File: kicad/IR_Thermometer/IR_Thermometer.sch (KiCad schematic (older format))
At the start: 17 parts, among them IC1 PIC16LF19156-I_SP, J1 ICSP Conn, J2 Sensor Conn, J3 Sensor Conn, Q1 SI2323, SW1 Sample Button, SW2 Option Button

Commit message: Updates to schematic
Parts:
- added R5: 100R, Resistors:0603, symbol Device:R
- C1: renamed from C2; value 100nF -> 100n
- C2: renamed from C3; value 100nF -> 100n
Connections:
- net GND: now also R5.1; no longer D1.1 (K)
- new net: D1.1 (K), R5.2
- no-connect marks 10 -> 9
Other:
- note added: "PMOSFET provides\nreverse battery\nprotection"
- moved on the sheet: C1, D1, IC1, R3, R4, SW1, SW2

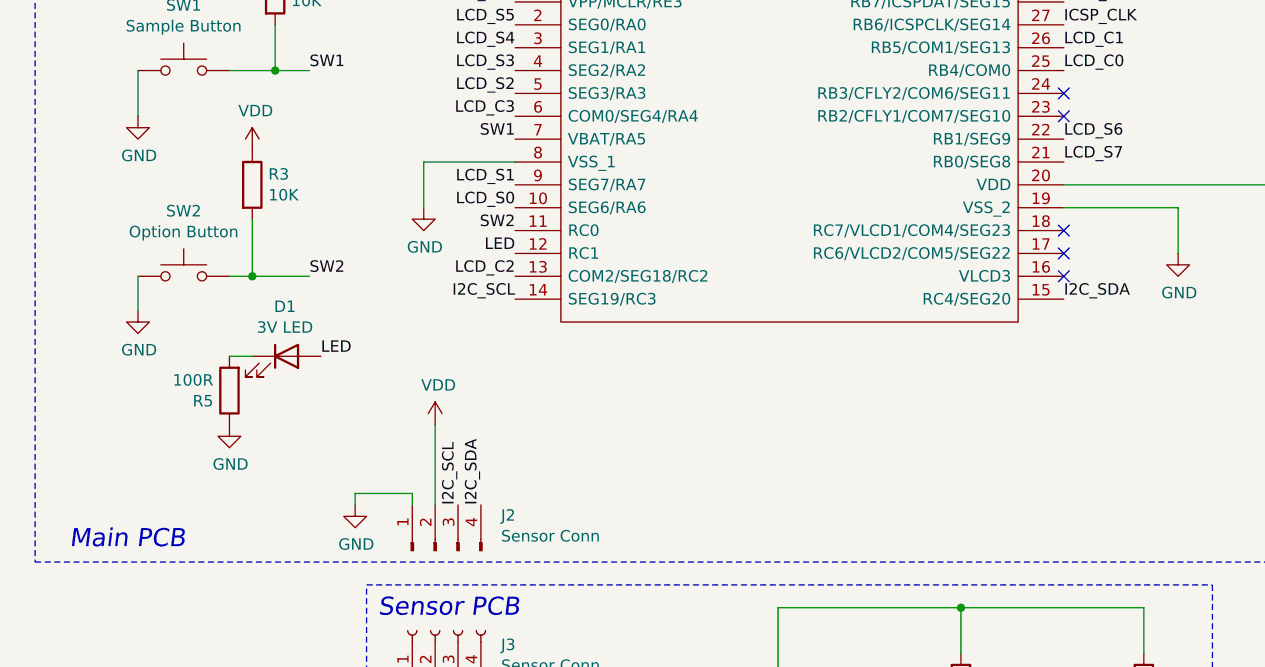
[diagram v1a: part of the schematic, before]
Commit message: Sleep mode implementation
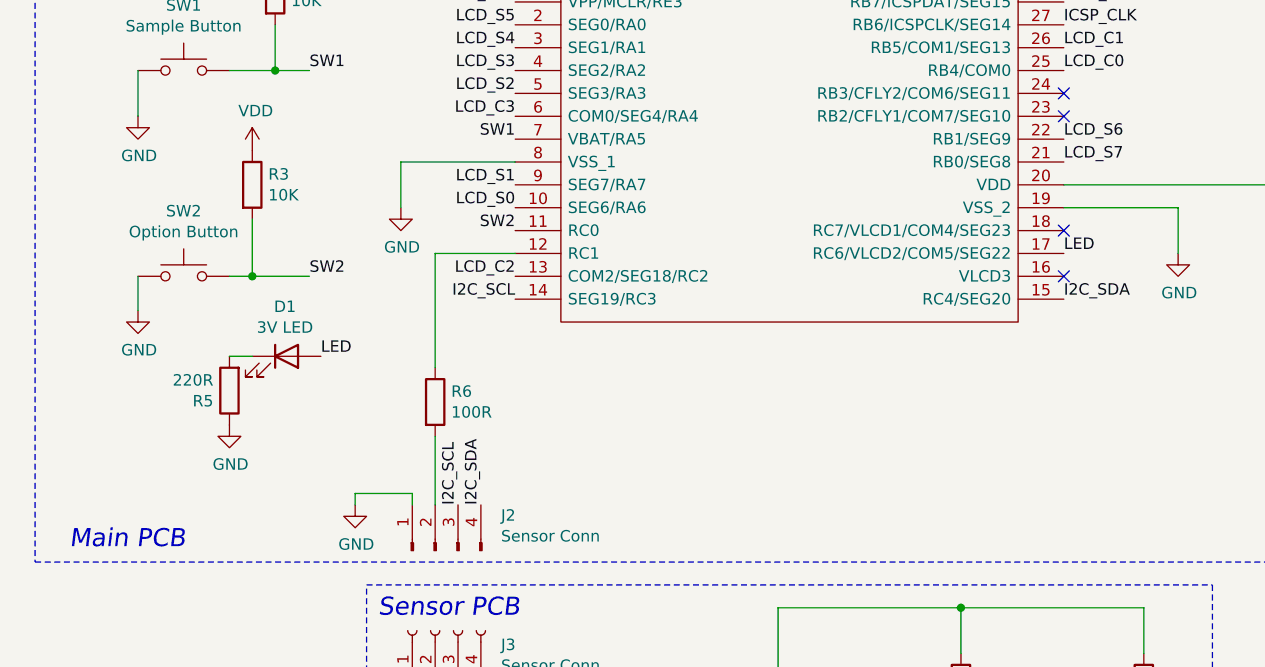
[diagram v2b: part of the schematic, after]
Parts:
- added R6: 100R, Resistor_THT:R_Axial_DIN0207_L6.3mm_D2.5mm_P2.54mm_Vertical, symbol Device:R
- C1: footprint Capacitors:0603 -> Capacitor_THT:C_Disc_D3.0mm_W1.6mm_P2.50mm
- C2: footprint Capacitors:0603 -> Capacitor_SMD:C_0603_1608Metric
- D1: footprint (none) -> LED_THT:LED_D3.0mm
- R1, R2: footprint Resistors:0603 -> Resistor_SMD:R_0603_1608Metric
- R3, R4: footprint Resistors:0603 -> Resistor_THT:R_Axial_DIN0207_L6.3mm_D2.5mm_P2.54mm_Vertical
- R5: value 100R -> 220R
- SW1, SW2: footprint FSM2JRT:FSM2JRT -> Button_Switch_THT:SW_TH_Tactile_Omron_B3F-10xx
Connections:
- net LED: now also IC1.17 (RC6/VLCD2/COM5/SEG22); no longer IC1.12 (RC1)
- net VDD: no longer J2.2 (Pin_2)
- new net: IC1.12 (RC1), R6.1
- new net: J2.2 (Pin_2), R6.2
- no-connect marks 9 -> 8
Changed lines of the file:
@@
 Sheet 1 1
 Title "Non-contact IR Thermometer"
-Date "2021-05-29"
-Rev "0.7"
+Date "2022-02-28"
+Rev "0.8"
 Comp "Karen A. Morrissey"
 Comment1 "A minimal part, low-power design for a non-contact IR thermometer."
@@
 F 0 "C1" H 6465 3296 50  0000 L CNN
 F 1 "100n" H 6465 3205 50  0000 L CNN
-F 2 "Capacitors:0603" H 6388 3100 50  0001 C CNN
+F 2 "Capacitor_THT:C_Disc_D3.0mm_W1.6mm_P2.50mm" H 6388 3100 50  0001 C CNN
 F 3 "~" H 6350 3250 50  0001 C CNN
 	1    6350 3250
 	1    0    0    -1
 $EndComp
-Wire Wire Line
-	2900 2850 2500 2850
 $Comp
 L Connector:Conn_01x06_Female J1
@@
 F 0 "SW2" H 1450 3635 50  0000 C CNN
 F 1 "Option Button" H 1450 3544 50  0000 C CNN
-F 2 "FSM2JRT:FSM2JRT" H 1450 3550 50  0001 C CNN
+F 2 "Button_Switch_THT:SW_TH_Tactile_Omron_B3F-10xx" H 1450 3550 50  0001 C CNN
 F 3 "~" H 1450 3550 50  0001 C CNN
 	1    1450 3350
@@
 F 0 "SW1" H 1450 2735 50  0000 C CNN
 F 1 "Sample Button" H 1450 2644 50  0000 C CNN
-F 2 "FSM2JRT:FSM2JRT" H 1450 2650 50  0001 C CNN
+F 2 "Button_Switch_THT:SW_TH_Tactile_Omron_B3F-10xx" H 1450 2650 50  0001 C CNN
 F 3 "~" H 1450 2650 50  0001 C CNN
 	1    1450 2450
@@
 L power:GND #PWR04
 U 1 1 6044CFCD
-P 2500 3050
-F 0 "#PWR04" H 2500 2800 50  0001 C CNN
-F 1 "GND" H 2505 2877 50  0000 C CNN
-F 2 "" H 2500 3050 50  0001 C CNN
-F 3 "" H 2500 3050 50  0001 C CNN
-	1    2500 3050
+P 2400 3050
+F 0 "#PWR04" H 2400 2800 50  0001 C CNN
+F 1 "GND" H 2405 2877 50  0000 C CNN
+F 2 "" H 2400 3050 50  0001 C CNN
+F 3 "" H 2400 3050 50  0001 C CNN
+	1    2400 3050
 	1    0    0    -1
 $EndComp
@@
 F 0 "R1" H 4920 5196 50  0000 L CNN
 F 1 "4.7K" H 4920 5105 50  0000 L CNN
-F 2 "Resistors:0603" V 4780 5150 50  0001 C CNN
+F 2 "Resistor_SMD:R_0603_1608Metric" V 4780 5150 50  0001 C CNN
 F 3 "~" H 4850 5150 50  0001 C CNN
 	1    4850 5150
@@
 F 0 "R2" H 5720 5196 50  0000 L CNN
 F 1 "4.7K" H 5720 5105 50  0000 L CNN
-F 2 "Resistors:0603" V 5580 5150 50  0001 C CNN
+F 2 "Resistor_SMD:R_0603_1608Metric" V 5580 5150 50  0001 C CNN
 F 3 "~" H 5650 5150 50  0001 C CNN
 	1    5650 5150
@@
 F 0 "C2" H 4165 6546 50  0000 L CNN
 F 1 "100n" H 4165 6455 50  0000 L CNN
-F 2 "Capacitors:0603" H 4088 6350 50  0001 C CNN
+F 2 "Capacitor_SMD:C_0603_1608Metric" H 4088 6350 50  0001 C CNN
 F 3 "~" H 4050 6500 50  0001 C CNN
 	1    4050 6500
@@
 	1    0    0    -1
 $EndComp
-$Comp
-L power:VDD #PWR08
-U 1 1 607F1EE9
-P 2550 4000
-F 0 "#PWR08" H 2550 3850 50  0001 C CNN
-F 1 "VDD" H 2565 4173 50  0000 C CNN
-F 2 "" H 2550 4000 50  0001 C CNN
-F 3 "" H 2550 4000 50  0001 C CNN
-	1    2550 4000
-	1    0    0    -1
-$EndComp
 Wire Wire Line
 	2650 5100 2650 7700
@@
 $EndComp
 Connection ~ 8150 3150
-Wire Wire Line
-	2550 4000 2550 4350
 Wire Notes Line
 	2250 4700 5950 4700
@@
 F 0 "R4" H 1920 2146 50  0000 L CNN
 F 1 "10K" H 1920 2055 50  0000 L CNN
-F 2 "Resistors:0603" V 1780 2100 50  0001 C CNN
+F 2 "Resistor_THT:R_Axial_DIN0207_L6.3mm_D2.5mm_P2.54mm_Vertical" V 1780 2100 50  0001 C CNN
 F 3 "~" H 1850 2100 50  0001 C CNN
 	1    1850 2100
@@
 F 0 "R3" H 1820 2996 50  0000 L CNN
 F 1 "10K" H 1820 2905 50  0000 L CNN
-F 2 "Resistors:0603" V 1680 2950 50  0001 C CNN
+F 2 "Resistor_THT:R_Axial_DIN0207_L6.3mm_D2.5mm_P2.54mm_Vertical" V 1680 2950 50  0001 C CNN
 F 3 "~" H 1750 2950 50  0001 C CNN
 	1    1750 2950
@@
 NoConn ~ 5300 2650
 NoConn ~ 5300 3150
-NoConn ~ 5300 3250
 Wire Notes Line
 	800  600  800  4600
@@
 	1850 2450 2000 2450
 Connection ~ 1850 2450
-Wire Wire Line
-	2500 2850 2500 3050
 Text Label 2900 2750 2    50   ~ 0
 SW1
@@
 F 0 "D1" H 1893 3917 50  0000 C CNN
 F 1 "3V LED" H 1893 3826 50  0000 C CNN
-F 2 "" H 1900 3700 50  0001 C CNN
+F 2 "LED_THT:LED_D3.0mm" H 1900 3700 50  0001 C CNN
 F 3 "~" H 1900 3700 50  0001 C CNN
 	1    1900 3700
@@
 Text Label 2050 3700 0    50   ~ 0
 LED
-Text Label 2900 3250 2    50   ~ 0
-LED
 Text Notes 7350 3850 0    50   ~ 0
 PMOSFET provides\nreverse battery\nprotection
@@
 P 1650 3850
 F 0 "R5" H 1720 3896 50  0000 L CNN
-F 1 "100R" H 1720 3805 50  0000 L CNN
+F 1 "220R" H 1720 3805 50  0000 L CNN
 F 2 "Resistors:0603" V 1580 3850 50  0001 C CNN
 F 3 "~" H 1650 3850 50  0001 C CNN
@@
 Wire Wire Line
 	1750 3700 1650 3700
+Text Label 5300 3250 0    50   ~ 0
+LED
+Wire Wire Line
+	2400 2850 2400 3050
+Wire Wire Line
+	2400 2850 2900 2850
+$Comp
+L Device:R R6
+U 1 1 621E9958
+P 2550 3900
+F 0 "R6" H 2620 3946 50  0000 L CNN
+F 1 "100R" H 2620 3855 50  0000 L CNN
+F 2 "Resistor_THT:R_Axial_DIN0207_L6.3mm_D2.5mm_P2.54mm_Vertical" V 2480 3900 50  0001 C CNN
+F 3 "~" H 2550 3900 50  0001 C CNN
+	1    2550 3900
+	1    0    0    -1
+$EndComp
+Wire Wire Line
+	2550 4350 2550 4050
+Wire Wire Line
+	2900 3250 2550 3250
+Wire Wire Line
+	2550 3250 2550 3750
 $EndSCHEMATC
